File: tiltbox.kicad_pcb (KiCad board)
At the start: 4 copper layers, 65 x 65 mm, 219 parts, among them J1 USB_C, J2 batt conn., J3 Conn_01x08_Socket, SW1 SW_Wuerth_450301014042, U1 ESP32-C3-WROOM-02, U2 ADXL343, U3 TP4056-42-ESOP8, U4 AMS1117-3.3

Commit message: moved esp
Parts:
- moved U1 3.74 mm to (133.8, 81.1)
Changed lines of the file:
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@@
 	(footprint "RF_Module:ESP32-C3-WROOM-02"
 		(layer "B.Cu")
-		(at 133.858 84.824)
+		(at 133.83 81.08)
 		(descr "RF Module, ESP32-C3 WROOM-02, Wi-Fi and Bluetooth, BLE, onboard antenna, https://www.espressif.com/sites/default/files/documentation/esp32-c3-wroom-02_datasheet_en.pdf")
 		(tags "ESP32-C3 WROOM-02 espressif")
@@
 			(polygon
 				(pts
-					(xy 119.858 91.924) (xy 147.858 91.924) (xy 147.858 102.924) (xy 119.858 102.924)
+					(xy 119.83 88.18) (xy 147.83 88.18) (xy 147.83 99.18) (xy 119.83 99.18)
 				)
 			)
@@
 		(end 95.36 100.175118)
 		(stroke
-			(width 0)
+			(width 0.1)
 			(type default)
 		)
@@
 		(end 98.312756 38.167244)
 		(stroke
-			(width 0)
+			(width 0.1)
 			(type default)
 		)
@@
 		(end 99.789134 41.12)
 		(stroke
-			(width 0)
+			(width 0.1)
 			(type default)
 		)
@@
 		(end 99.789134 100.175118)
 		(stroke
-			(width 0)
+			(width 0.1)
 			(type default)
 		)
@@
 		(end 95.36 100.175118)
 		(stroke
-			(width 0)
+			(width 0.1)
 			(type default)
 		)
@@
 		(end 98.312756 38.167244)
 		(stroke
-			(width 0)
+			(width 0.1)
 			(type default)
 		)
@@
 		(end 160.32063 41.12)
 		(stroke
-			(width 0)
+			(width 0.1)
 			(type default)
 		)
@@
 		(end 158.844252 41.12)
 		(stroke
-			(width 0)
+			(width 0.1)
 			(type default)
 		)
@@
 		(end 158.844252 100.175118)
 		(stroke
-			(width 0)
+			(width 0.1)
 			(type default)
 		)
@@
 		(end 98.312756 103.127874)
 		(stroke
-			(width 0)
+			(width 0.1)
 			(type default)
 		)
@@
 		(end 160.32063 100.175118)
 		(stroke
-			(width 0)
+			(width 0.1)
 			(type default)
 		)
@@
 		(end 157.367874 103.127874)
 		(stroke
-			(width 0)
+			(width 0.1)
 			(type default)
 		)

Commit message: verqndering
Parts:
- moved LED38 8.99 mm to (133.5, 59.8)
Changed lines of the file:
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@@
 	(footprint "LED_SMD:LED_WS2812B-Mini_PLCC4_3.5x3.5mm"
 		(layer "F.Cu")
-		(at 141.925 62.947089 180)
+		(at 133.51 59.79 180)
 		(descr "Addressable RGB LED NeoPixel Mini, 12 mA, https://web.archive.org/web/20200131233647/http://www.world-semi.com/DownLoadFile/112")
 		(tags "LED RGB NeoPixel Mini")

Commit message: verder gewerkt aan pcb
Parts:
- moved U2 32.1 mm to (151.7, 85.9), turned to 0 degrees
- moved U1 10.6 mm to (134.1, 91.6)
- moved LED38 8.96 mm to (141.9, 62.9)
- turned LED63 to 0 degrees
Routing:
- net GND: track 449.0 -> 571.4 mm, vias 0 -> 2
- net +5V: track 427.3 -> 517.6 mm
- net +3.3V: track 0.00 -> 79.0 mm
- net Din_LED: track 0.00 -> 62.9 mm, vias 0 -> 1
- net SDA: track 0.00 -> 45.2 mm
- net SCL: track 0.00 -> 42.5 mm
- net Net-(D1-A): track 0.00 -> 36.7 mm
- net Net-(U3-~{CHRG}): track 0.00 -> 35.3 mm
- net battery output 5v: track 0.00 -> 28.1 mm
- net Net-(U3-~{STDBY}): track 0.00 -> 20.5 mm
- net Net-(U3-PROG): track 0.00 -> 17.9 mm
- net 5v output: track 0.00 -> 17.0 mm
- net Net-(LED51-DO): track 0.00 -> 6.35 mm
- net Net-(LED71-DO): track 0.00 -> 6.35 mm
- net Net-(LED11-DO): track 0.00 -> 6.35 mm
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
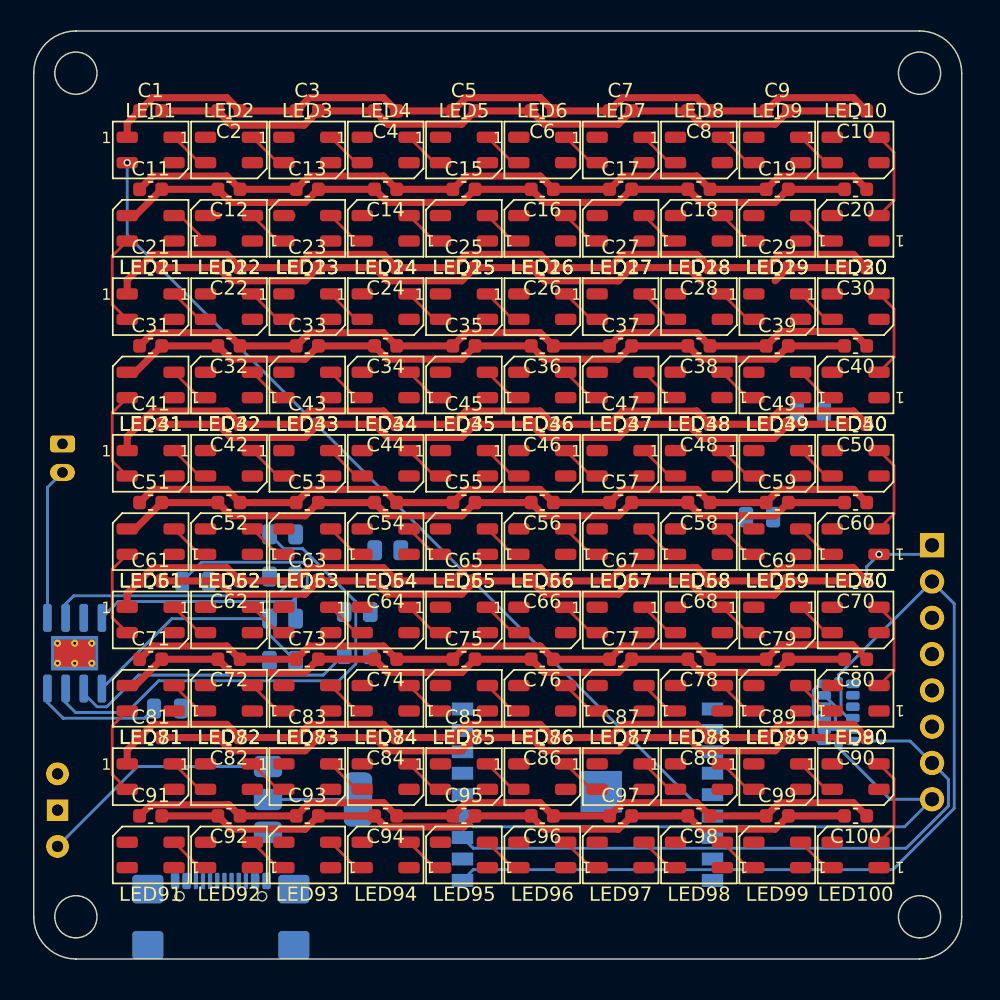
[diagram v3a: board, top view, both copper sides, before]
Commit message: ceep out zone
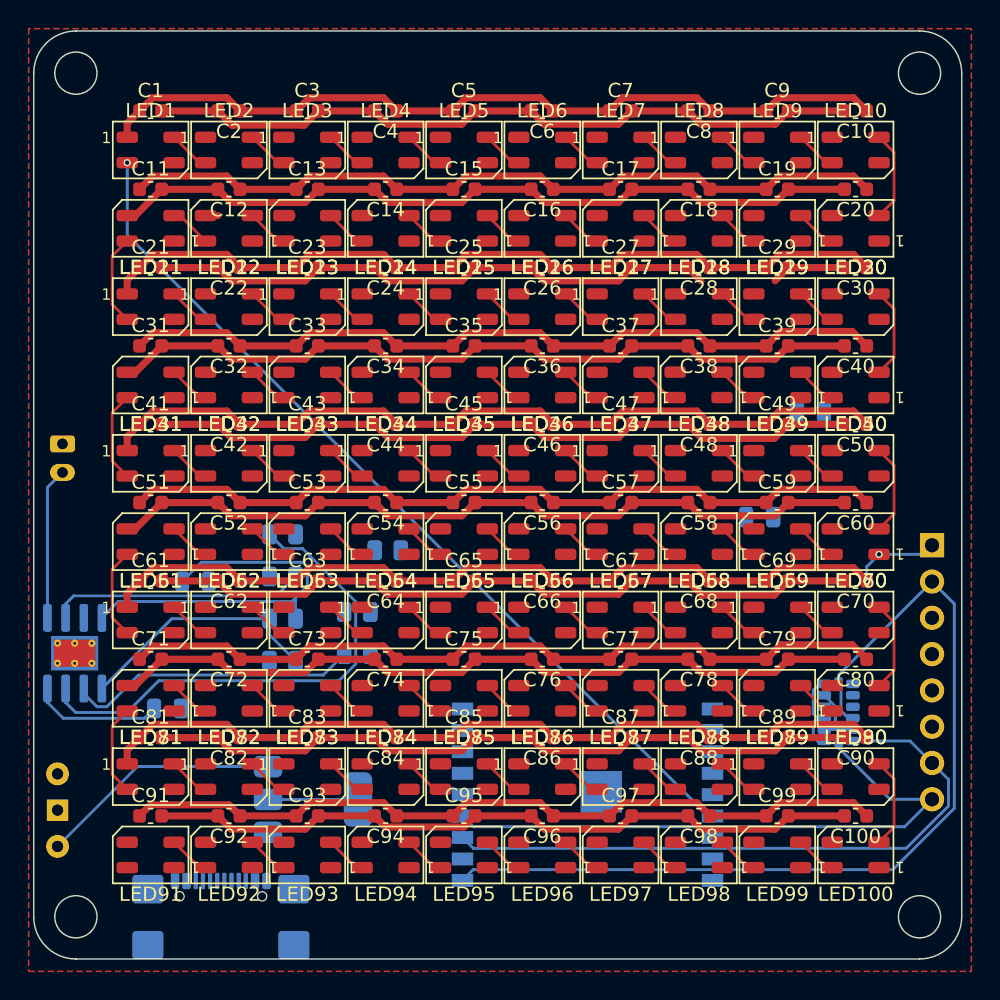
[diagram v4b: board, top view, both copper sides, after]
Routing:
- added copper zone on F.Cu, net +5V
- added copper zone on F.Cu, net GND
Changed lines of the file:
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@@
 	)
 	(zone
-		(locked yes)
+		(net "+5V")
+		(layer "F.Cu")
+		(name "+5v")
+		(hatch edge 0.5)
+		(connect_pads
+			(clearance 0)
+		)
+		(min_thickness 0.25)
+		(fill
+			(thermal_gap 0.5)
+			(thermal_bridge_width 0.5)
+			(island_removal_mode 0)
+		)
+		(polygon
+			(pts
+				(xy 161 38) (xy 95 38) (xy 95 104) (xy 161 104)
+			)
+		)
+	)
+	(zone
+		(net "GND")
+		(layer "F.Cu")
+		(name "gnd")
+		(hatch edge 0.5)
+		(priority 1)
+		(connect_pads
+			(clearance 0)
+		)
+		(min_thickness 0.25)
+		(fill
+			(thermal_gap 0.5)
+			(thermal_bridge_width 0.5)
+			(island_removal_mode 0)
+		)
+		(polygon
+			(pts
+				(xy 161 38) (xy 95 38) (xy 95 104) (xy 161 104)
+			)
+		)
+	)
+	(zone
 		(layer "B.CrtYd")
 		(name "ceep aut")
@@
 		(polygon
 			(pts
-				(xy 119.858 102.924) (xy 147.858 102.924) (xy 147.858 91.924) (xy 119.858 91.924)
+				(xy 119.815252 109.908618) (xy 148.377393 109.976508) (xy 148.377393 98.476508) (xy 119.877393 98.476508)
 			)
 		)
